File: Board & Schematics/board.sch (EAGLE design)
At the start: 16 parts, among them U1 ATTINY-85

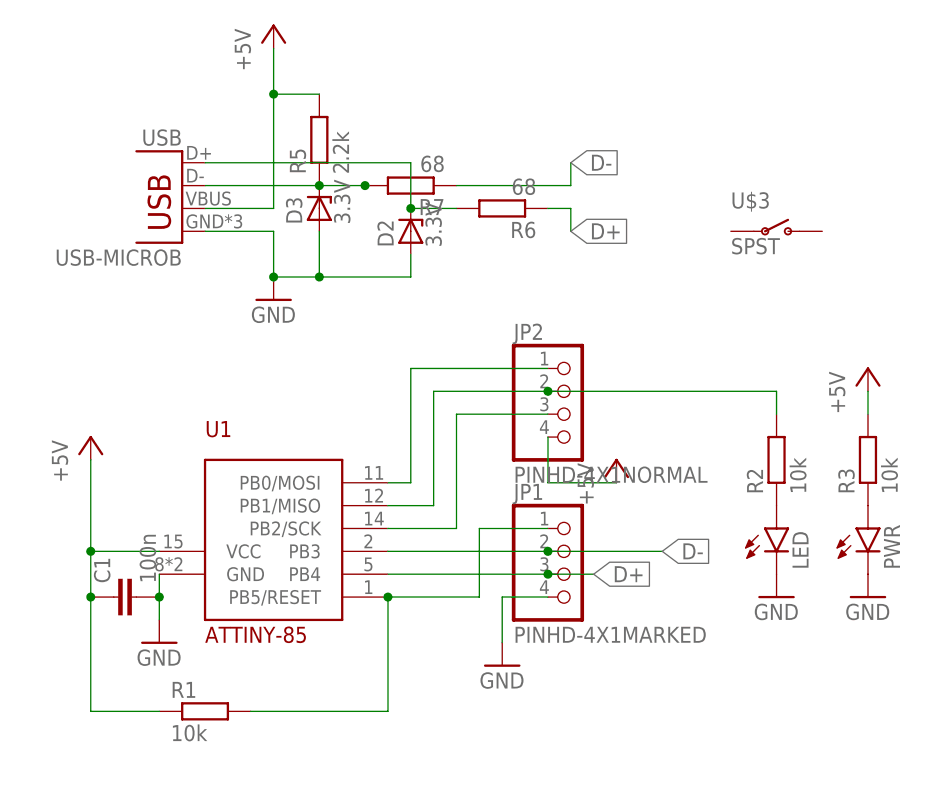
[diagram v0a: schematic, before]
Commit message: added reset switch to support bootloader
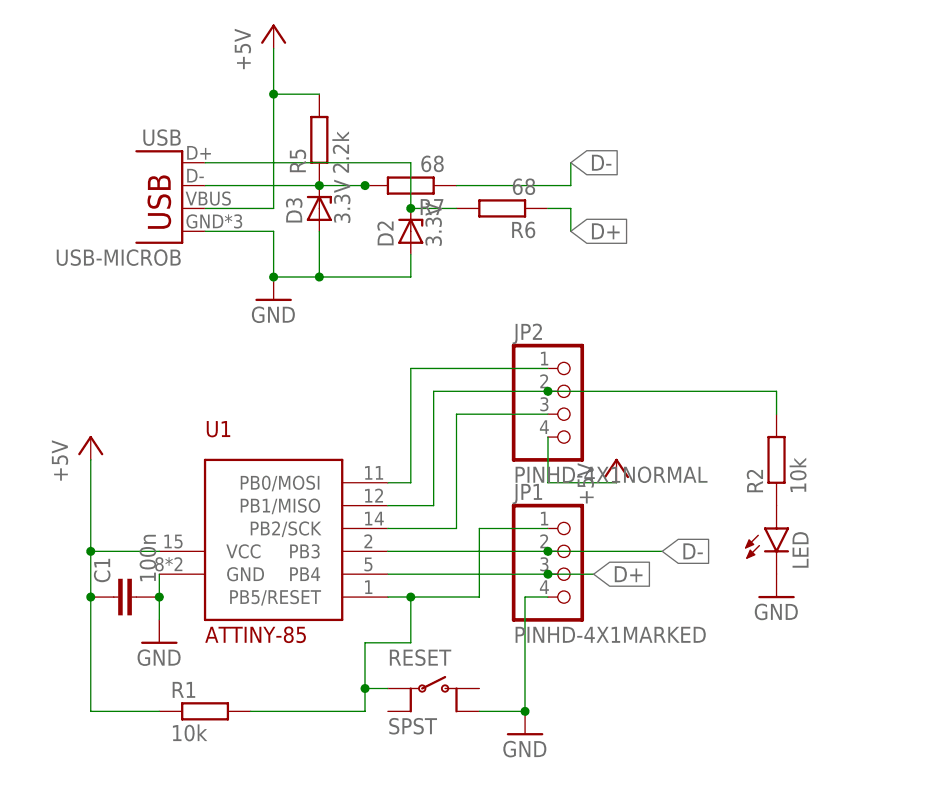
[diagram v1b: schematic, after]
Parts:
- removed PWR: (no value), SparkFun-LED:LED0603
- removed R3: 10k, rcl:R-EU_R0402
- removed U$3: SPST, OwnStuff:SPST
- added RESET: SPST, OwnStuff:SPST
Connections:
- removed net N$1: JP1.1, R1.2, U1.PB5/RESET
- removed net N$2: PWR.A, R3.1
- new net N$3: JP1.1, R1.2, RESET.P, U1.PB5/RESET
- net +5V: no longer R3.2
- net GND: now also RESET.O2; no longer PWR.C
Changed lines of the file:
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@@
 <part name="R6" library="rcl" deviceset="R-EU_" device="R0402" value="68"/>
 <part name="R7" library="rcl" deviceset="R-EU_" device="R0402" value="68"/>
-<part name="PWR" library="SparkFun-LED" deviceset="LED" device="0603"/>
-<part name="R3" library="rcl" deviceset="R-EU_" device="R0402" value="10k"/>
-<part name="GND4" library="supply1" deviceset="GND" device=""/>
-<part name="P+3" library="supply1" deviceset="+5V" device=""/>
-<part name="U$3" library="OwnStuff" deviceset="SPST" device=""/>
+<part name="RESET" library="OwnStuff" deviceset="SPST" device=""/>
 </parts>
 <sheets>
@@
 <instance part="GND1" gate="1" x="22.86" y="10.16"/>
 <instance part="C1" gate="G$1" x="17.78" y="15.24" rot="R90"/>
-<instance part="GND2" gate="1" x="60.96" y="7.62"/>
+<instance part="GND2" gate="1" x="63.5" y="0"/>
 <instance part="P+2" gate="1" x="73.66" y="30.48"/>
 <instance part="LED" gate="G$1" x="91.44" y="22.86"/>
@@
 <instance part="R6" gate="G$1" x="60.96" y="58.42" rot="R180"/>
 <instance part="R7" gate="G$1" x="50.8" y="60.96" rot="R180"/>
-<instance part="PWR" gate="G$1" x="101.6" y="22.86"/>
-<instance part="R3" gate="G$1" x="101.6" y="30.48" rot="R90"/>
-<instance part="GND4" gate="1" x="101.6" y="15.24"/>
-<instance part="P+3" gate="1" x="101.6" y="40.64"/>
-<instance part="U$3" gate="G$1" x="91.44" y="55.88"/>
+<instance part="RESET" gate="G$1" x="53.34" y="5.08"/>
 </instances>
 <busses>
 </busses>
 <nets>
-<net name="N$1" class="0">
-<segment>
-<pinref part="R1" gate="G$1" pin="2"/>
-<pinref part="U1" gate="G$1" pin="PB5/RESET"/>
-<wire x1="33.02" y1="2.54" x2="48.26" y2="2.54" width="0.1524" layer="91"/>
-<wire x1="48.26" y1="2.54" x2="48.26" y2="15.24" width="0.1524" layer="91"/>
-<wire x1="48.26" y1="15.24" x2="58.42" y2="15.24" width="0.1524" layer="91"/>
-<wire x1="58.42" y1="15.24" x2="58.42" y2="22.86" width="0.1524" layer="91"/>
-<junction x="48.26" y="15.24"/>
-<pinref part="JP1" gate="G$1" pin="1"/>
-<wire x1="58.42" y1="22.86" x2="66.04" y2="22.86" width="0.1524" layer="91"/>
-</segment>
-</net>
 <net name="GND" class="0">
 <segment>
@@
 <pinref part="JP1" gate="G$1" pin="4"/>
 <pinref part="GND2" gate="1" pin="GND"/>
-<wire x1="66.04" y1="15.24" x2="60.96" y2="15.24" width="0.1524" layer="91"/>
-<wire x1="60.96" y1="15.24" x2="60.96" y2="10.16" width="0.1524" layer="91"/>
+<wire x1="66.04" y1="15.24" x2="63.5" y2="15.24" width="0.1524" layer="91"/>
+<wire x1="63.5" y1="15.24" x2="63.5" y2="2.54" width="0.1524" layer="91"/>
+<pinref part="RESET" gate="G$1" pin="O2"/>
+<wire x1="58.42" y1="2.54" x2="63.5" y2="2.54" width="0.1524" layer="91"/>
+<junction x="63.5" y="2.54"/>
 </segment>
 <segment>
@@
 <junction x="40.64" y="50.8"/>
 </segment>
-<segment>
-<pinref part="PWR" gate="G$1" pin="C"/>
-<pinref part="GND4" gate="1" pin="GND"/>
-</segment>
 </net>
 <net name="N$4" class="0">
@@
 <wire x1="66.04" y1="27.94" x2="66.04" y2="33.02" width="0.1524" layer="91"/>
 </segment>
-<segment>
-<pinref part="P+3" gate="1" pin="+5V"/>
-<pinref part="R3" gate="G$1" pin="2"/>
-<wire x1="101.6" y1="38.1" x2="101.6" y2="35.56" width="0.1524" layer="91"/>
-</segment>
 </net>
 <net name="N$7" class="0">
@@
 </segment>
 </net>
-<net name="N$2" class="0">
-<segment>
-<pinref part="PWR" gate="G$1" pin="A"/>
-<pinref part="R3" gate="G$1" pin="1"/>
-</segment>
-</net>
+<net name="N$3" class="0">
+<segment>
+<wire x1="45.72" y1="2.54" x2="45.72" y2="5.08" width="0.1524" layer="91"/>
+<pinref part="U1" gate="G$1" pin="PB5/RESET"/>
+<wire x1="45.72" y1="5.08" x2="45.72" y2="10.16" width="0.1524" layer="91"/>
+<wire x1="48.26" y1="15.24" x2="50.8" y2="15.24" width="0.1524" layer="91"/>
+<wire x1="50.8" y1="15.24" x2="58.42" y2="15.24" width="0.1524" layer="91"/>
+<wire x1="58.42" y1="15.24" x2="58.42" y2="22.86" width="0.1524" layer="91"/>
+<pinref part="JP1" gate="G$1" pin="1"/>
+<wire x1="58.42" y1="22.86" x2="66.04" y2="22.86" width="0.1524" layer="91"/>
+<wire x1="45.72" y1="10.16" x2="50.8" y2="10.16" width="0.1524" layer="91"/>
+<wire x1="50.8" y1="10.16" x2="50.8" y2="15.24" width="0.1524" layer="91"/>
+<junction x="50.8" y="15.24"/>
+<pinref part="RESET" gate="G$1" pin="P"/>
+<wire x1="48.26" y1="5.08" x2="45.72" y2="5.08" width="0.1524" layer="91"/>
+<junction x="45.72" y="5.08"/>
+<pinref part="R1" gate="G$1" pin="2"/>
+<wire x1="45.72" y1="2.54" x2="33.02" y2="2.54" width="0.1524" layer="91"/>
+</segment>
+</net>
